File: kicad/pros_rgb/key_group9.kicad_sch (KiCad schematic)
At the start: 16 parts

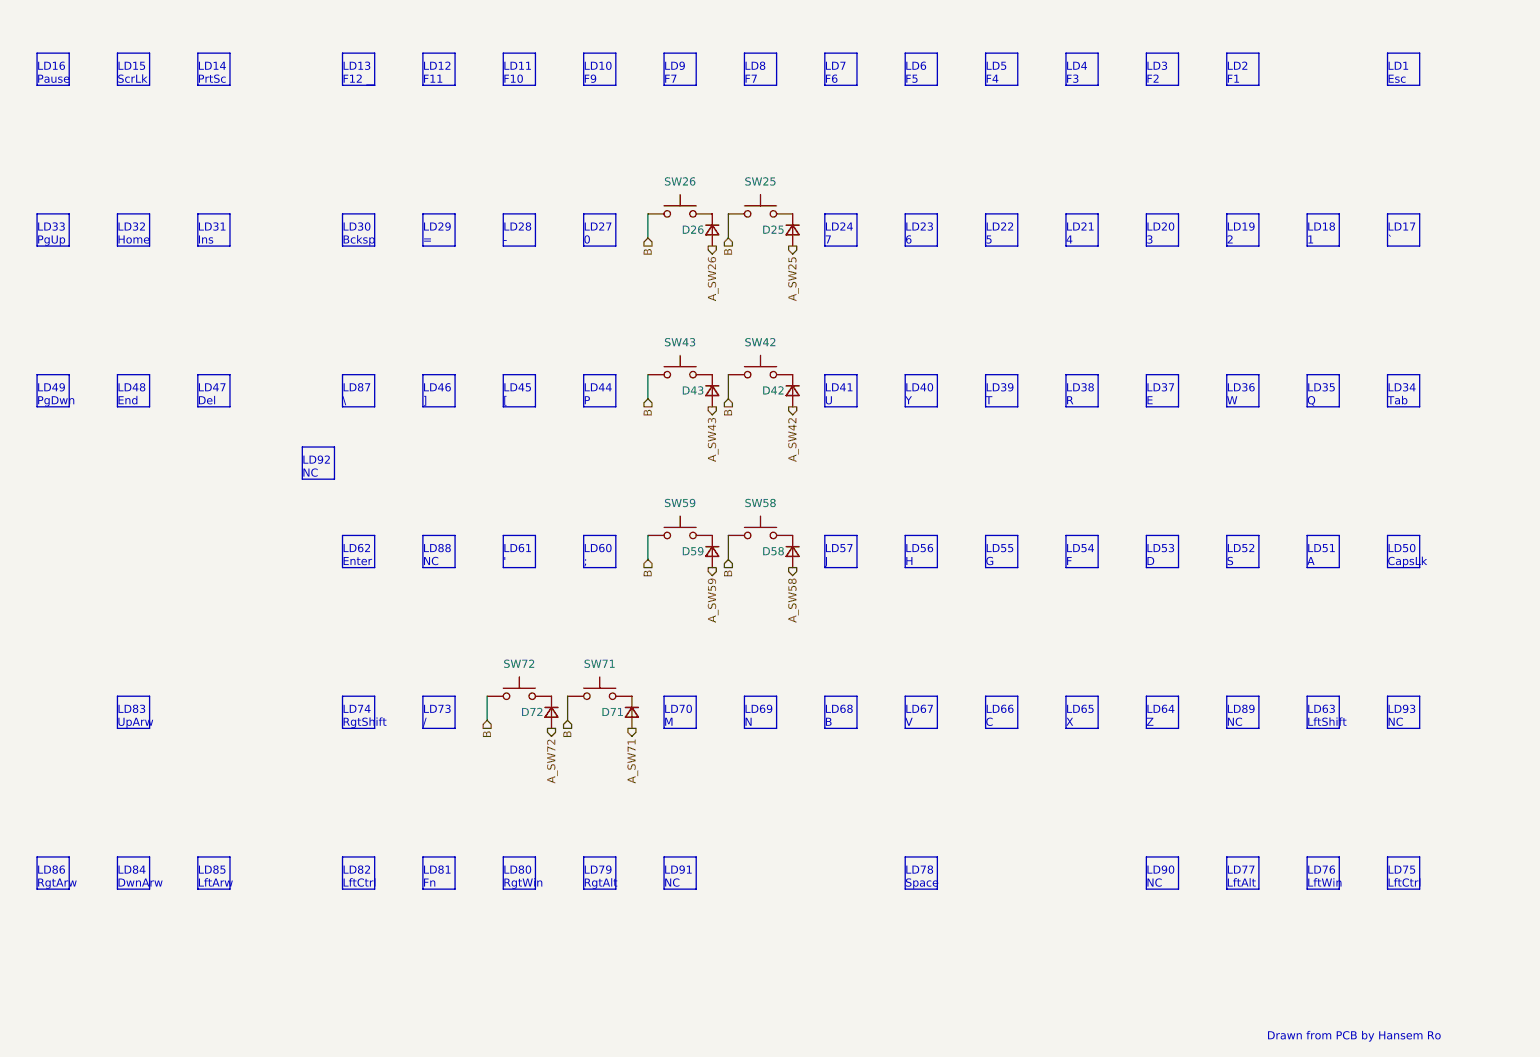
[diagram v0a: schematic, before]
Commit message: kicad/pros_rgb: update key groupings
These new groupings are based off ordering in firmware:
https://github.com/hansemro/pok3r_re_firmware/blob/4b68aa4baf7d28dc8dbf8eebcb1fdb59e7bcd629/disassemble/cmprosrgb/v122/cmprosrgb_v122.txt#L14599-L14629
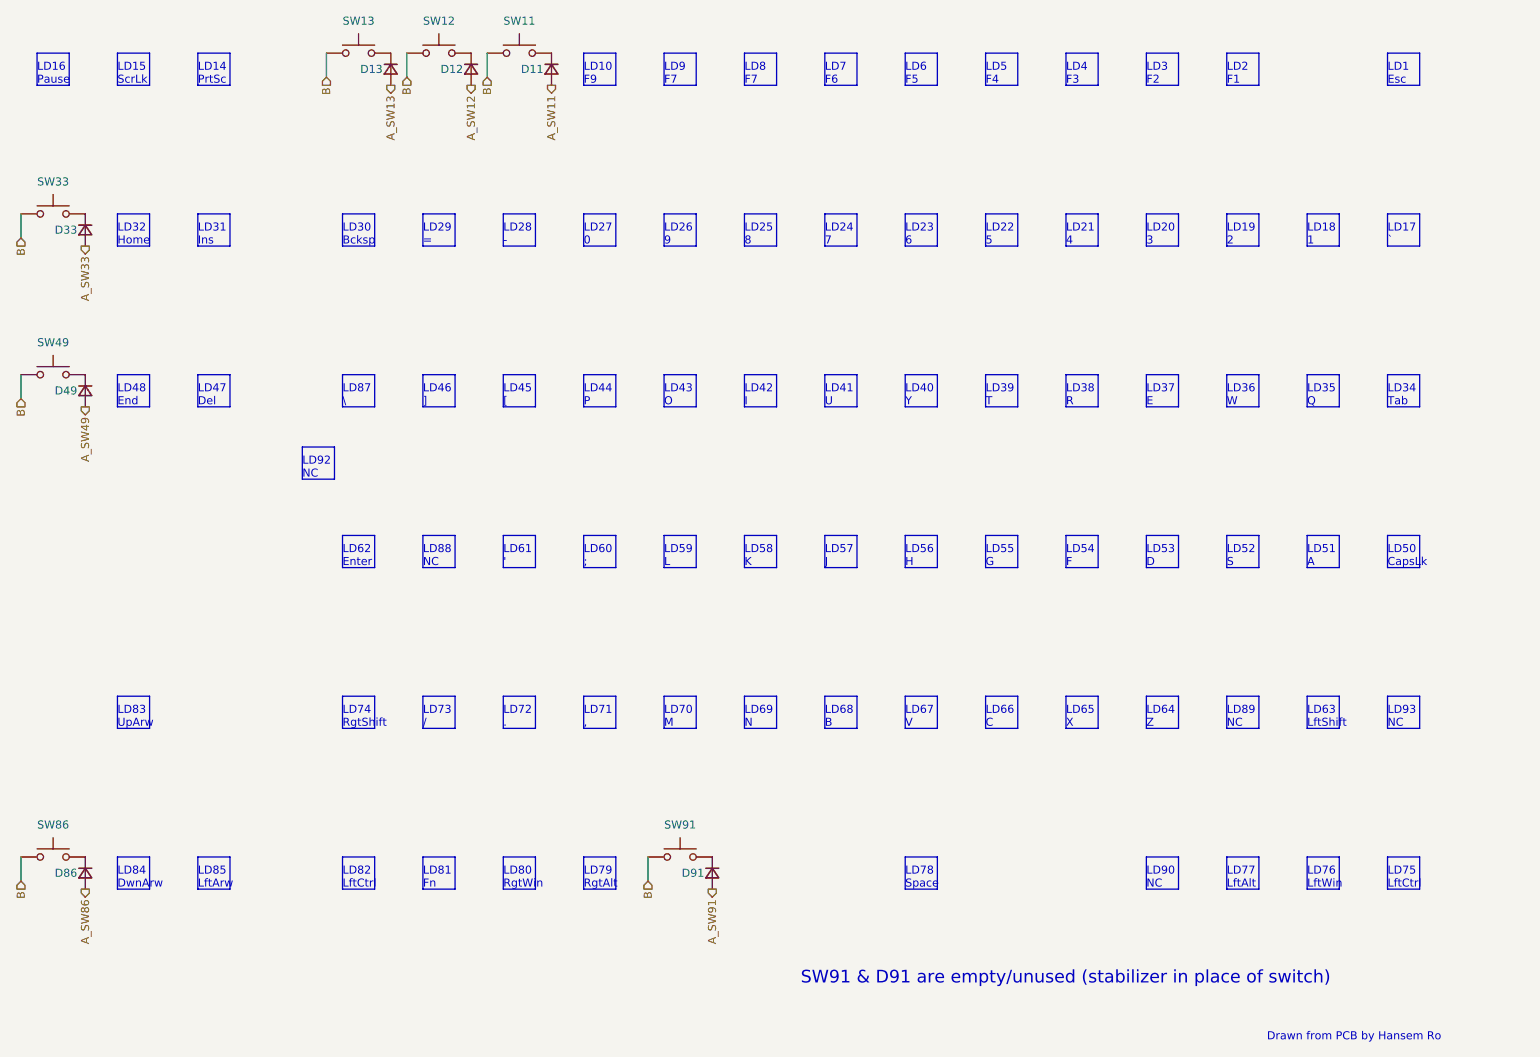
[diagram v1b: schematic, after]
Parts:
- removed D25, D26, D42, D43, D58, D59, D71, D72: ~, symbol Device:D_Small
- removed SW25, SW26, SW42, SW43, SW58, SW59, SW71, SW72: ~, symbol Switch:SW_Push
- added D11, D12, D13, D33, D49, D86, D91: (no value), symbol Device:D_Small
- added SW11, SW12, SW13, SW33, SW49, SW86, SW91: (no value), symbol Switch:SW_Push
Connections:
- net B: now also SW11.1, SW12.1, SW13.1, SW33.1, SW49.1, SW86.1, SW91.1
- new net: D86.1 (K), SW86.2
- new net: D91.1 (K), SW91.2
- new net: D49.1 (K), SW49.2
- new net: D33.1 (K), SW33.2
- new net: D11.1 (K), SW11.2
- new net: D13.1 (K), SW13.2
- new net: D12.1 (K), SW12.2
- new net A_SW11: D11.2 (A)
- new net A_SW12: D12.2 (A)
- new net A_SW13: D13.2 (A)
- new net A_SW33: D33.2 (A)
- new net A_SW49: D49.2 (A)
- new net A_SW86: D86.2 (A)
- new net A_SW91: D91.2 (A)
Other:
- note added: "LD25 8"
- note added: "LD26 9"
- note added: "LD42 I"
- note added: "LD43 O"
- note added: "LD58 K"
- note added: "LD59 L"
- note added: "LD71 ,"
- note added: "LD72 ."
- note added: "SW91 & D91 are empty/unused (stabilizer in place of switch)"
- note removed: "LD11 F10"
- note removed: "LD12 F11"
- note removed: "LD13 F12"
- note removed: "LD33 PgUp"
- note removed: "LD49 PgDwn"
- note removed: "LD86 RgtArw"
- note removed: "LD91 NC"

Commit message: kicad/pros_rgb: mark as Rev. B
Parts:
- D11, D12, D13, D33, D49, D86, D91, SW11, SW12, SW13, SW33, SW49, SW86, SW91: value (none) -> ~
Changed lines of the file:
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@@
     (in_bom yes) (on_board yes)
     (property "Reference" "SW86" (id 0) (at 60.96 146.05 0))
-    (property "Value" "" (id 1) (at 60.96 146.05 0))
+    (property "Value" "~" (id 1) (at 60.96 146.05 0))
     (property "Footprint" "" (id 2) (at 60.96 146.05 0)
       (effects (font (size 1.27 1.27)) hide)
@@
       (effects (font (size 1.27 1.27)) (justify right))
     )
-    (property "Value" "" (id 1) (at 167.64 154.9399 90)
+    (property "Value" "~" (id 1) (at 167.64 154.9399 90)
       (effects (font (size 1.27 1.27)) (justify left))
     )
@@
     (in_bom yes) (on_board yes)
     (property "Reference" "SW49" (id 0) (at 60.96 69.85 0))
-    (property "Value" "" (id 1) (at 60.96 69.85 0))
+    (property "Value" "~" (id 1) (at 60.96 69.85 0))
     (property "Footprint" "" (id 2) (at 60.96 69.85 0)
       (effects (font (size 1.27 1.27)) hide)
@@
       (effects (font (size 1.27 1.27)) (justify right))
     )
-    (property "Value" "" (id 1) (at 68.58 53.3399 90)
+    (property "Value" "~" (id 1) (at 68.58 53.3399 90)
       (effects (font (size 1.27 1.27)) (justify left))
     )
@@
       (effects (font (size 1.27 1.27)) (justify right))
     )
-    (property "Value" "" (id 1) (at 142.24 27.9399 90)
+    (property "Value" "~" (id 1) (at 142.24 27.9399 90)
       (effects (font (size 1.27 1.27)) (justify left))
     )
@@
     (in_bom yes) (on_board yes)
     (property "Reference" "SW11" (id 0) (at 134.62 19.05 0))
-    (property "Value" "" (id 1) (at 134.62 19.05 0))
+    (property "Value" "~" (id 1) (at 134.62 19.05 0))
     (property "Footprint" "" (id 2) (at 134.62 19.05 0)
       (effects (font (size 1.27 1.27)) hide)
@@
     (in_bom yes) (on_board yes)
     (property "Reference" "SW13" (id 0) (at 109.22 19.05 0))
-    (property "Value" "" (id 1) (at 109.22 19.05 0))
+    (property "Value" "~" (id 1) (at 109.22 19.05 0))
     (property "Footprint" "" (id 2) (at 109.22 19.05 0)
       (effects (font (size 1.27 1.27)) hide)
@@
     (in_bom yes) (on_board yes)
     (property "Reference" "SW33" (id 0) (at 60.96 44.45 0))
-    (property "Value" "" (id 1) (at 60.96 44.45 0))
+    (property "Value" "~" (id 1) (at 60.96 44.45 0))
     (property "Footprint" "" (id 2) (at 60.96 44.45 0)
       (effects (font (size 1.27 1.27)) hide)
@@
       (effects (font (size 1.27 1.27)) (justify right))
     )
-    (property "Value" "" (id 1) (at 68.58 154.9399 90)
+    (property "Value" "~" (id 1) (at 68.58 154.9399 90)
       (effects (font (size 1.27 1.27)) (justify left))
     )
@@
     (in_bom yes) (on_board yes)
     (property "Reference" "SW12" (id 0) (at 121.92 19.05 0))
-    (property "Value" "" (id 1) (at 121.92 19.05 0))
+    (property "Value" "~" (id 1) (at 121.92 19.05 0))
     (property "Footprint" "" (id 2) (at 121.92 19.05 0)
       (effects (font (size 1.27 1.27)) hide)
@@
       (effects (font (size 1.27 1.27)) (justify right))
     )
-    (property "Value" "" (id 1) (at 116.84 27.9399 90)
+    (property "Value" "~" (id 1) (at 116.84 27.9399 90)
       (effects (font (size 1.27 1.27)) (justify left))
     )
@@
       (effects (font (size 1.27 1.27)) (justify right))
     )
-    (property "Value" "" (id 1) (at 129.54 27.9399 90)
+    (property "Value" "~" (id 1) (at 129.54 27.9399 90)
       (effects (font (size 1.27 1.27)) (justify left))
     )
@@
     (in_bom yes) (on_board yes)
     (property "Reference" "SW91" (id 0) (at 160.02 146.05 0))
-    (property "Value" "" (id 1) (at 160.02 146.05 0))
+    (property "Value" "~" (id 1) (at 160.02 146.05 0))
     (property "Footprint" "" (id 2) (at 160.02 146.05 0)
       (effects (font (size 1.27 1.27)) hide)
@@
       (effects (font (size 1.27 1.27)) (justify right))
     )
-    (property "Value" "" (id 1) (at 68.58 78.7399 90)
-      (effects (font (size 1.27 1.27)) (justify left))
-    )
+    (property "Value" "~" (id 1) (at 68.58 78.7399 90)
+      (effects (font (size 1.27 1.27)) (justify left))
+    )

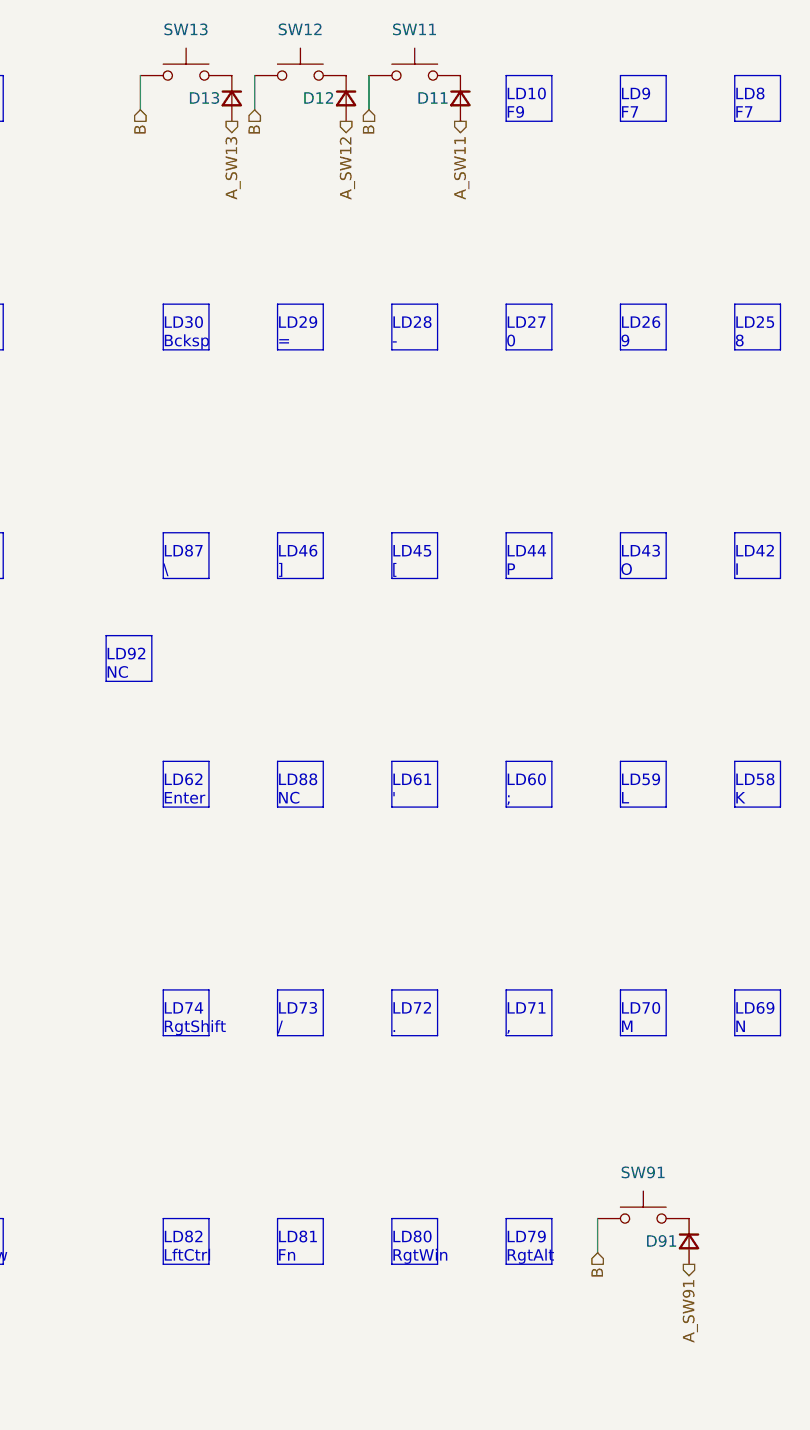
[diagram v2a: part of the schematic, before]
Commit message: kicad/pros_rgb: fix typos
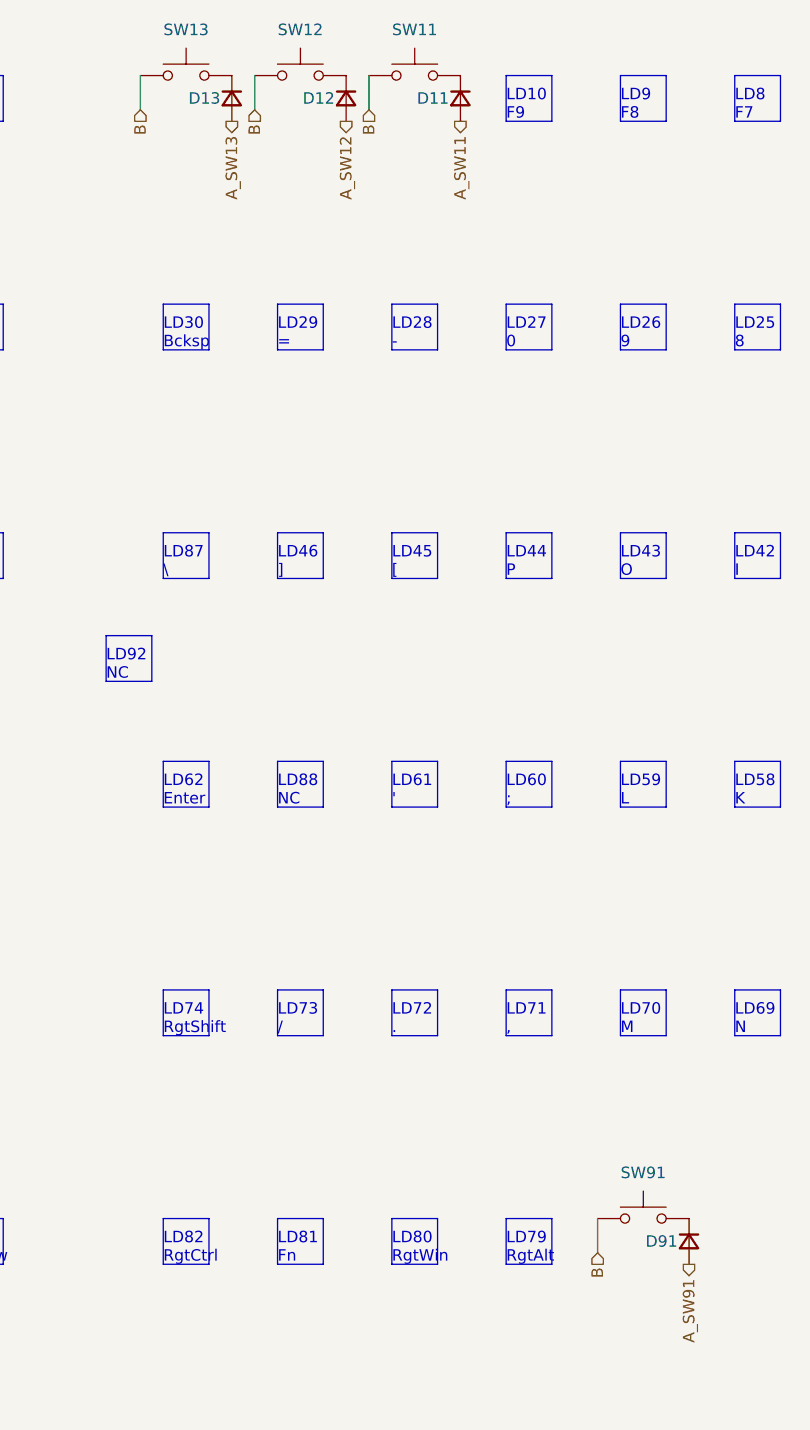
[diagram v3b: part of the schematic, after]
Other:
- note added: "LD82 RgtCtrl"
- note added: "LD9 F8"
- note removed: "LD82 LftCtrl"
- note removed: "LD9 F7"
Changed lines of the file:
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@@
     (effects (font (size 1.27 1.27)) (justify left bottom))
   )
-  (text "LD9\nF7" (at 157.48 29.21 0)
+  (text "LD9\nF8" (at 157.48 29.21 0)
     (effects (font (size 1.27 1.27)) (justify left bottom))
   )
@@
     (effects (font (size 1.27 1.27)) (justify left bottom))
   )
-  (text "LD82\nLftCtrl" (at 106.68 156.21 0)
+  (text "LD82\nRgtCtrl" (at 106.68 156.21 0)
     (effects (font (size 1.27 1.27)) (justify left bottom))
   )
